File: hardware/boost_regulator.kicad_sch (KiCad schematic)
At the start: 0 parts

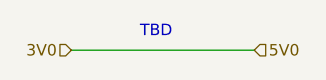
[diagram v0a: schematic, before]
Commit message: hardware: Add Q2 to prevent discharging battery from 5V_SOLAR net, misc cleanup
The body diode of Q1 allowed current to be conducted back into the solar
panel. This is something that can happen during the night in a typical
solar panel circuit. I don't know what our solar panel module looks like
internally so add this just in case.
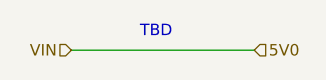
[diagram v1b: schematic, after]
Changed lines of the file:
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@@
   (paper "A4")
   (title_block
-    (date "2022-01-20")
-    (rev "0.0.1")
+    (date "2022-02-07")
+    (rev "0.0.2")
   )
   (wire (pts (xy 149.86 82.55) (xy 170.18 82.55))
@@
     (effects (font (size 1.27 1.27)) (justify left))
   )
-  (hierarchical_label "3V0" (shape input) (at 149.86 82.55 180)
+  (hierarchical_label "VIN" (shape input) (at 149.86 82.55 180)
     (effects (font (size 1.27 1.27)) (justify right))
   )
